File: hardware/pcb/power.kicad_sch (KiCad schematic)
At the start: 1 part, among them IC1 MCP16502

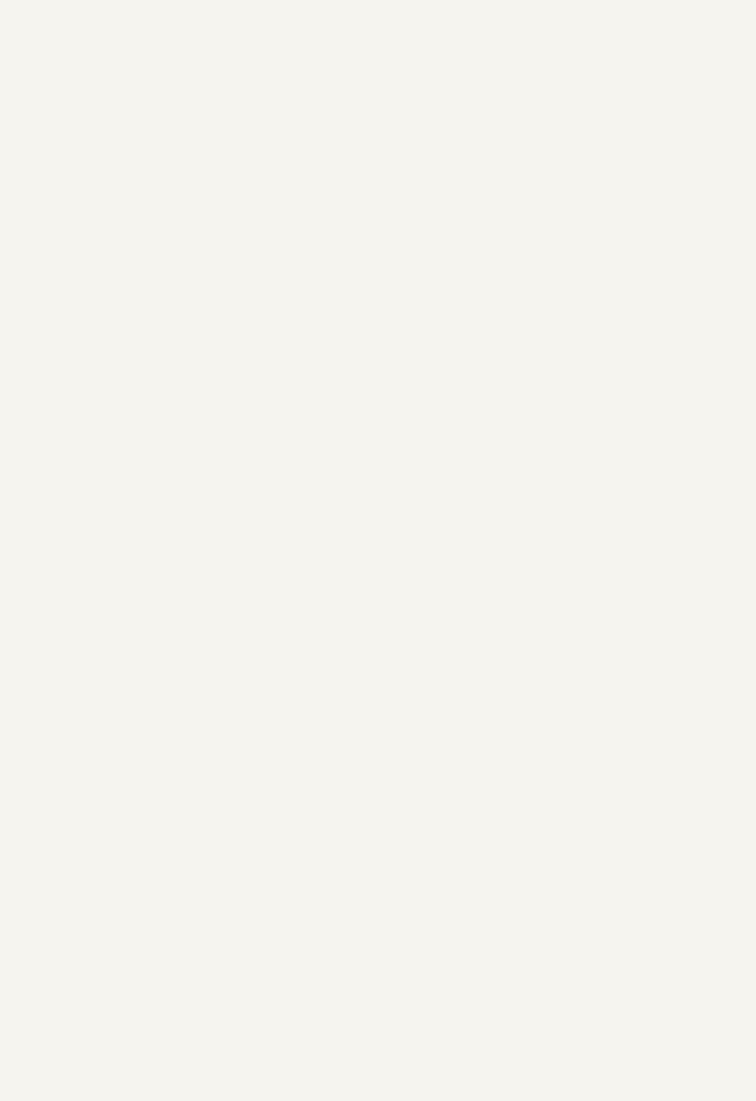
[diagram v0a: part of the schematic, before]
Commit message: created MAX17260 and BQ25640 symbols
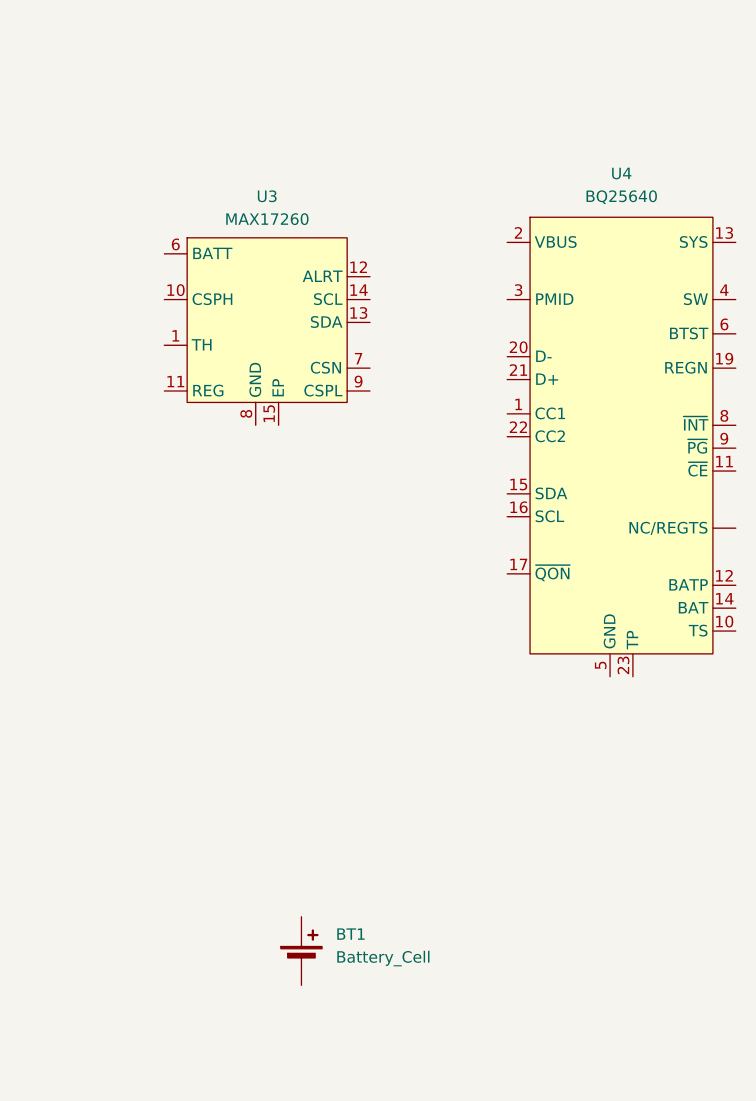
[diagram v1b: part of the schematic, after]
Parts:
- added BT1: Battery_Cell, symbol Device:Battery_Cell
- added U3: MAX17260, Package_DFN_QFN:TDFN-14-1EP_3x3mm_P0.4mm_EP1.78x2.35mm, symbol MAX17260:MAX17260
- added U4: BQ25640, symbol BQ25640:BQ25640
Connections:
- new net: U3.2 (NC), U3.3 (NC), U3.4 (NC), U3.5 (NC)
- new net GND: U4.18 (GND), U4.5 (GND)

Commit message: usb power
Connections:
- net GND: now also IC1.33 (EP), U3.15 (EP), U3.8 (GND), U4.23 (TP)
- net CC1: now reaches U4.1 (CC1)
- net SDA: now reaches U4.15 (SDA)
- net SDA: now also IC1.5 (SDA), U3.14 (SCL)
- net SCL: now reaches U4.16 (SCL)
- net SCL: now also IC1.6 (SCL), U3.13 (SDA)
- net VBUS: now reaches U4.2 (VBUS)
- net CC2: now reaches U4.22 (CC2)
- no-connect marks 0 -> 2
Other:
- note added: "0x36/0x1A"
- note added: "0x5B"
- note added: "0x6B"
- moved on the sheet: BT1, IC1, U3, U4

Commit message: finished power
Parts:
- added C10, C11, C13, C15, C17, C18, C19: 4u7, symbol Device:C_Small
- added C12, C14, C16, C5, C9: 22u, symbol Device:C_Small
- added C2, C20: 1u, symbol Device:C_Small
- added C3: 10u, symbol Device:C_Small
- added C4: 47n, symbol Device:C_Small
- added C6: 20u, symbol Device:C_Small
- added C7: 470n, symbol Device:C_Small
- added C8: 100n, symbol Device:C_Small
- added D5: LED, LED_SMD:LED_0603_1608Metric, symbol Device:LED_Small
- added JP1: SolderJumper_2_Open, symbol Jumper:SolderJumper_2_Open
- added L1, L2, L3, L4, L5: 2uH, symbol Device:L_Small
- added R3: 100R, symbol Device:R_Small
- added R4: 10m, symbol Device:R_Small
- added R5: 1k5, symbol Device:R_Small
- added SW0: SW_Push, symbol Switch:SW_Push
- IC1: value MCP16502 -> MCP16502AD
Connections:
- net GND: now also IC1.12 (PGND1), IC1.13 (PGND2), IC1.17 (SELV2), IC1.18 (SELVL1), IC1.28 (PGND3), IC1.29 (PGND4), IC1.3 (SGND), U3.7 (CSN), C10.2, C11.2, C12.2, C13.2, C14.2, C15.2, C16.2, C17.2, C18.2, C19.2, C2.2, C20.2, C3.2, C5.2, C6.2, C7.2, C8.2, C9.2, JP1.1 (A), R4.2, SW0.1
- net VBUS: now also C2.1
- net at U4.12 (BATP): now also R3.1
- net +VSYS: now reaches U4.13 (SYS)
- net +VSYS: now also IC1.10 (PVIN1), IC1.15 (PVIN2), IC1.20 (LVIN), IC1.26 (PVIN3), IC1.31 (PVIN4), IC1.4 (SVIN), C10.1, C11.1, C13.1, C15.1, C17.1, C20.1, C5.1, D5.2 (A), L1.2
- net +BATT: now reaches U4.14 (BAT)
- net +BATT: now also BT1.1 (+), U3.1 (TH), U3.10 (CSPH), U3.6 (BATT), C8.1, R3.2
- net at U4.17 (~{QON}): now also JP1.2 (B)
- net at U4.19 (REGN): now also C6.1
- net at U4.3 (PMID): now also C3.1
- net at U4.4 (SW): now also C4.1, L1.1
- net at U4.6 (BTST): now also C4.2
- net CHG_~{INT}: now reaches U4.8 (~{INT})
- net at U4.9 (~{PG}): now also R5.1
- net NINTO: now reaches IC1.1 (NINTO)
- net at IC1.11 (SW1): now also L2.1
- net at IC1.14 (SW2): now also L3.1
- net +1V2_DDR: now reaches IC1.16 (OUT2)
- net +1V2_DDR: now also C12.1, L3.2
- net +BATT_CPU: now reaches IC1.19 (LOUT1)
- net +BATT_CPU: now also C18.1
- net NRSTO: now reaches IC1.2 (NRSTO)
- net +1V8: now reaches IC1.21 (LOUT2)
- net +1V8: now also C19.1
- net LPM: now reaches IC1.22 (LPM)
- net HPM: now reaches IC1.23 (HPM)
- net at IC1.24 (NSTRT): now also SW0.2
- net +1V15_CORE: now reaches IC1.25 (OUT3)
- net +1V15_CORE: now also C14.1, L4.2
- net at IC1.27 (SW3): now also L4.1
- net at IC1.30 (SW4): now also L5.1
- net +1V15_CPU: now reaches IC1.32 (OUT4)
- net +1V15_CPU: now also C16.1, L5.2
- net NSTRTO: now reaches IC1.7 (NSTRTO)
- net PWRHOLD: now reaches IC1.8 (PWRHLD)
- net +3V3: now reaches IC1.9 (OUT1)
- net +3V3: now also C9.1, L2.2
- net at BT1.2 (-): now also U3.9 (CSPL), R4.1
- net at U3.11 (REG): now also C7.1
- net FUEL_~{INT}: now reaches U3.12 (ALRT)
- new net: D5.1 (K), R5.2
- no-connect marks 2 -> 5
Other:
- note added: "1A"
- note added: "BMS"
- note added: "FUEL GAUGE & BATTERY"
- note added: "PMIC"
- moved on the sheet: BT1, IC1, U3, U4

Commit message: contiunued working
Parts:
- IC1: MPN (none) -> MCP16502AD; Manufacturer_Name Microchip -> (none); Manufacturer_Part_Number MCP16502TAE-E/S8B -> (none); Mouser Part Number 579-MCP16502TAEE/S8B -> (none); Mouser Price/Stock https://www.mouser.co.uk/ProductDetail/Microchip-Technology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 -> (none)
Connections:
- net +BATT_CPU renamed +1V8_BATT_CPU
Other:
- note removed: "1A"

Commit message: small stuff with mpu
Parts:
- added C26: 100n, symbol Device:C_Small
- added R6, R7, R8: 10k, symbol Device:R_Small
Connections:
- net +3V3: now also R6.2, R7.2
- net +VSYS: now also R8.2
- net GND: now also C26.1
- net at L1.1, U4.4 (SW): now also C4.2; no longer C4.1
- net at U4.6 (BTST): now also C4.1; no longer C4.2
- net at IC1.24 (NSTRT), SW0.2: now also C26.2
- net NINTO renamed ~{INT}
- net ~{INT}: now also R6.1
- net NRSTO renamed ~{RST}
- net ~{RST}: now also R7.1
- net NSTRTO renamed ~{WKUP}
- net ~{WKUP}: now also R8.1
- net PWRHOLD renamed PWRHLD
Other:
- moved on the sheet: C10, C11, C12, C13, C14, C15, C16, C17, C18, C19, C20, C4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

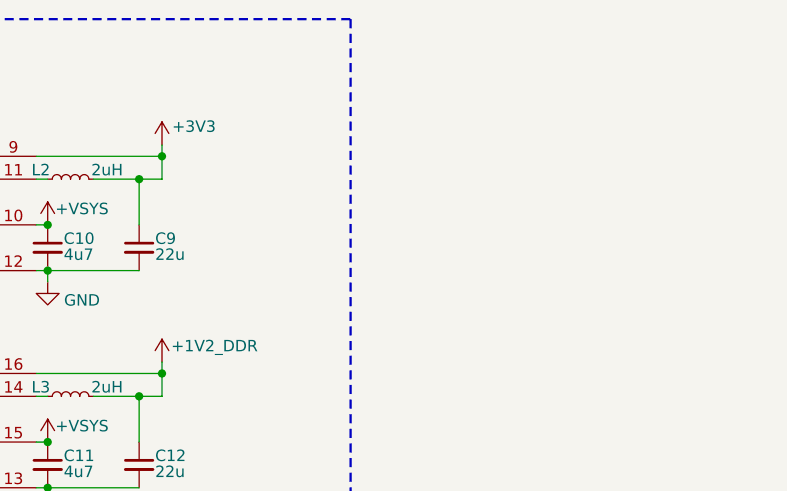
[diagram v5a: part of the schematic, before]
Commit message: bunch of small audio changes
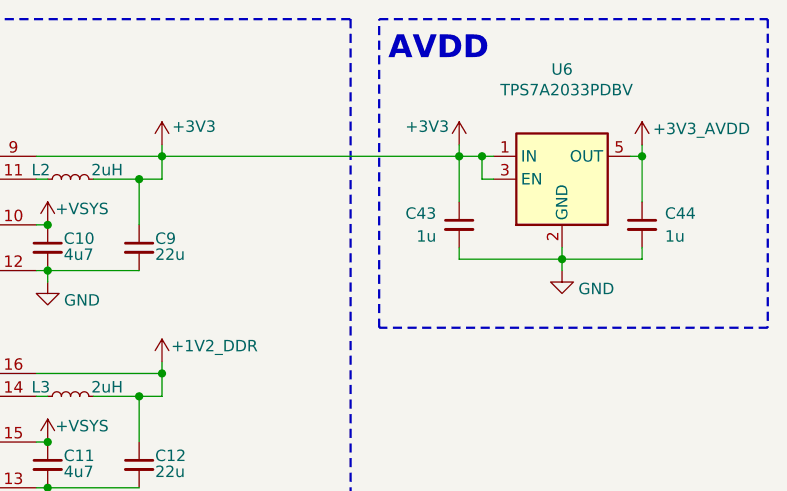
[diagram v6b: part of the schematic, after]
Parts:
- added C43, C44: 1u, symbol Device:C_Small
- added U6: TPS7A2033PDBV, Package_TO_SOT_SMD:SOT-23-5, symbol Regulator_Linear:TPS7A20xxxDBV
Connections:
- net +3V3: now also C43.1, U6.1 (IN), U6.3 (EN)
- net GND: now also C43.2, C44.2, U6.2 (GND)
- new net +3V3_AVDD: C44.1, U6.5 (OUT)
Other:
- note added: "AVDD"

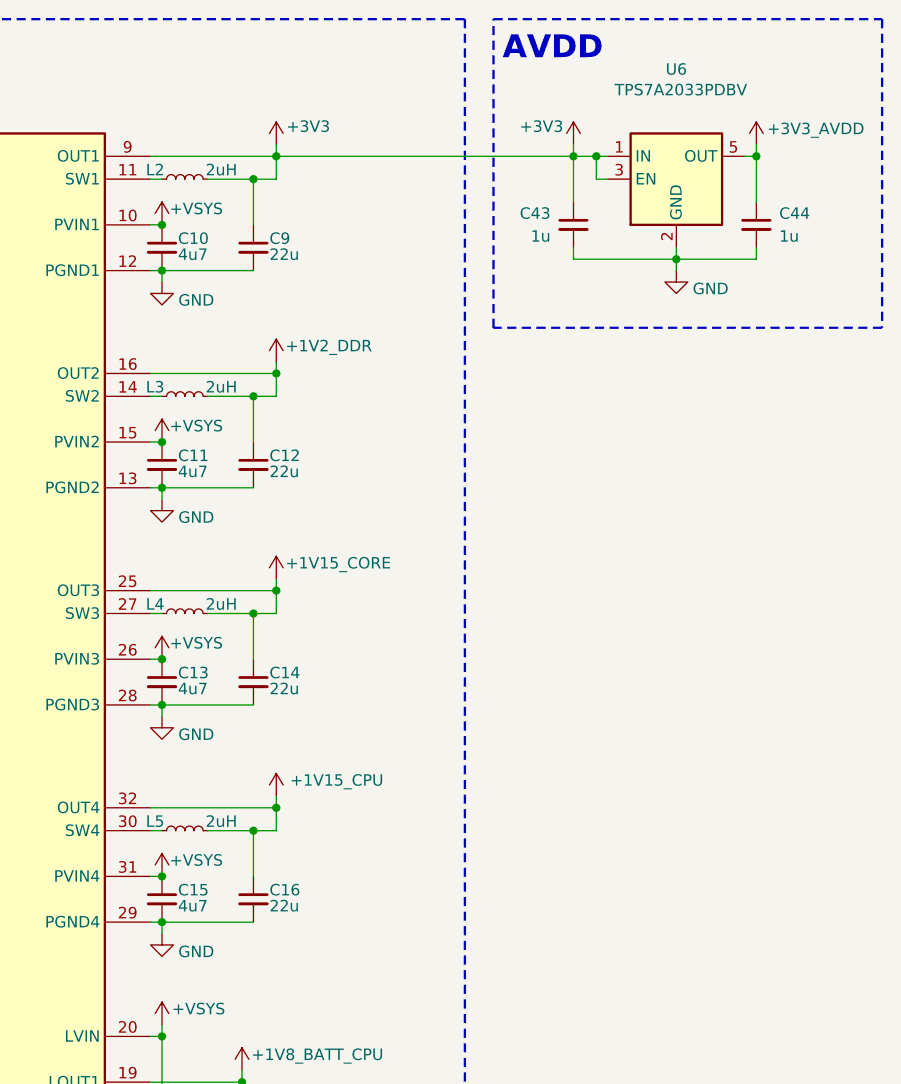
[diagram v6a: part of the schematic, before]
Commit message: bunch of small audio changes
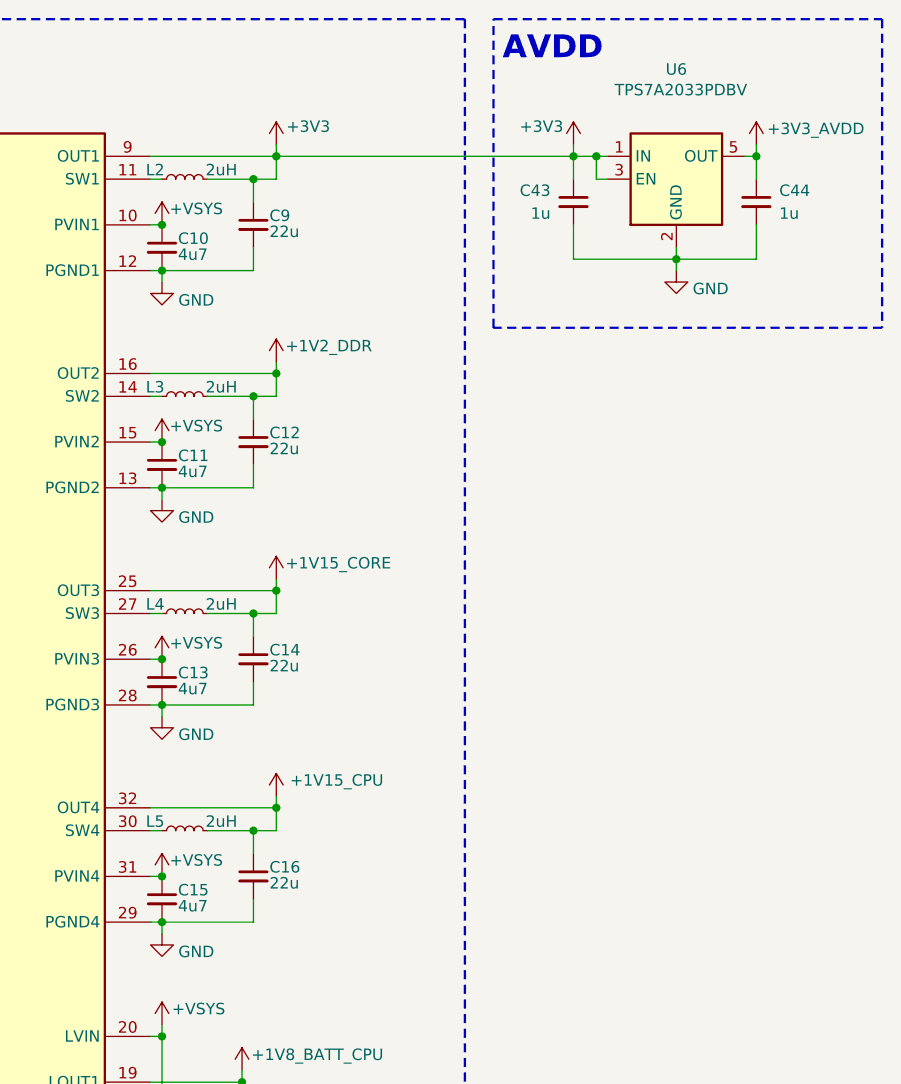
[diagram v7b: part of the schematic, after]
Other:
- moved on the sheet: C12, C14, C16, C43, C44, C9

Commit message: replaced lpddr3 with ddr3l
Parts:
- IC1: value MCP16502AD -> MCP16502AB; Height 1 -> (none); MPN MCP16502AD -> MCP16502AB
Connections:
- net GND: no longer IC1.17 (SELV2)
- net +1V2_DDR renamed +1V35_DDR
- no-connect marks 5 -> 6
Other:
- note added: "1V35 for DDR"
- note added: "1V8 for LOUT1"
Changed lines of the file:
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@@
 		)
 	)
+	(text "1V35 for DDR"
+		(exclude_from_sim no)
+		(at 192.024 183.134 0)
+		(effects
+			(font
+				(size 1.27 1.27)
+			)
+			(justify right)
+		)
+	)
 	(text "PMIC"
 		(exclude_from_sim no)
@@
 		)
 	)
+	(text "1V8 for LOUT1"
+		(exclude_from_sim no)
+		(at 188.976 187.96 0)
+		(effects
+			(font
+				(size 1.27 1.27)
+			)
+			(justify right)
+		)
+	)
 	(text "FUEL GAUGE & BATTERY"
 		(exclude_from_sim no)
@@
 	)
 	(junction
-		(at 193.04 187.96)
-		(diameter 0)
-		(color 0 0 0 0)
-	)
-	(junction
 		(at 299.72 80.01)
 		(diameter 0)
@@
 	)
 	(no_connect
+		(at 194.31 182.88)
+	)
+	(no_connect
 		(at 90.17 92.71)
 	)
@@
 	(wire
 		(pts
-			(xy 194.31 182.88) (xy 193.04 182.88)
-		)
-		(stroke
-			(width 0)
-			(type default)
-		)
-	)
-	(wire
-		(pts
 			(xy 80.01 85.09) (xy 80.01 83.82)
 		)
@@
 	(wire
 		(pts
-			(xy 193.04 182.88) (xy 193.04 187.96)
-		)
-		(stroke
-			(width 0)
-			(type default)
-		)
-	)
-	(wire
-		(pts
 			(xy 261.62 106.68) (xy 264.16 106.68)
 		)
@@
 			)
 		)
-		(property "Value" "MCP16502AD"
+		(property "Value" "MCP16502AB"
 			(at 222.25 74.93 0)
 			(show_name no)
@@
 			)
 		)
-		(property "Height" "1"
-			(at 254 519.38 0)
-			(hide yes)
-			(show_name no)
-			(do_not_autoplace no)
-			(effects
-				(font
-					(size 1.27 1.27)
-				)
-				(justify left top)
-			)
-		)
-		(property "Arrow Part Number" ""
-			(at 254 1019.38 0)
-			(hide yes)
-			(show_name no)
-			(do_not_autoplace no)
-			(effects
-				(font
-					(size 1.27 1.27)
-				)
-				(justify left top)
-			)
-		)
-		(property "Arrow Price/Stock" ""
-			(at 254 1119.38 0)
-			(hide yes)
-			(show_name no)
-			(do_not_autoplace no)
-			(effects
-				(font
-					(size 1.27 1.27)
-				)
-				(justify left top)
-			)
-		)
-		(property "MPN" "MCP16502AD"
-			(at 222.25 134.62 0)
-			(hide yes)
-			(show_name no)
-			(do_not_autoplace no)
-			(effects
-				(font
-					(size 1.27 1.27)
-				)
-			)
-		)
-		(property "KLC_S3.3" ""
-			(at 222.25 134.62 0)
-			(hide yes)
-			(show_name no)
-			(do_not_autoplace no)
-			(effects
-				(font
-					(size 1.27 1.27)
-				)
-			)
-		)
-		(property "KLC_S4.1" ""
+		(property "MPN" "MCP16502AB"
 			(at 222.25 134.62 0)
 			(hide yes)
@@
 			)
 		)
-		(property "Value" "+1V2_DDR"
+		(property "Value" "+1V35_DDR"
 			(at 265.176 101.092 0)
 			(show_name no)
